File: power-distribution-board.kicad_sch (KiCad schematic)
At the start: 18 parts, among them J1 703W-00_52, J10 12V, J11 12V, J12 12V, J13 12V, J14 12V, J15 5V, J16 5V, J17 5V, J2 Screw_Terminal_01x03, J3 Screw_Terminal_01x03, J4 Screw_Terminal_01x03, J5 12V, J6 12V, J7 12V, J8 12V, J9 12V, U1 IP2721

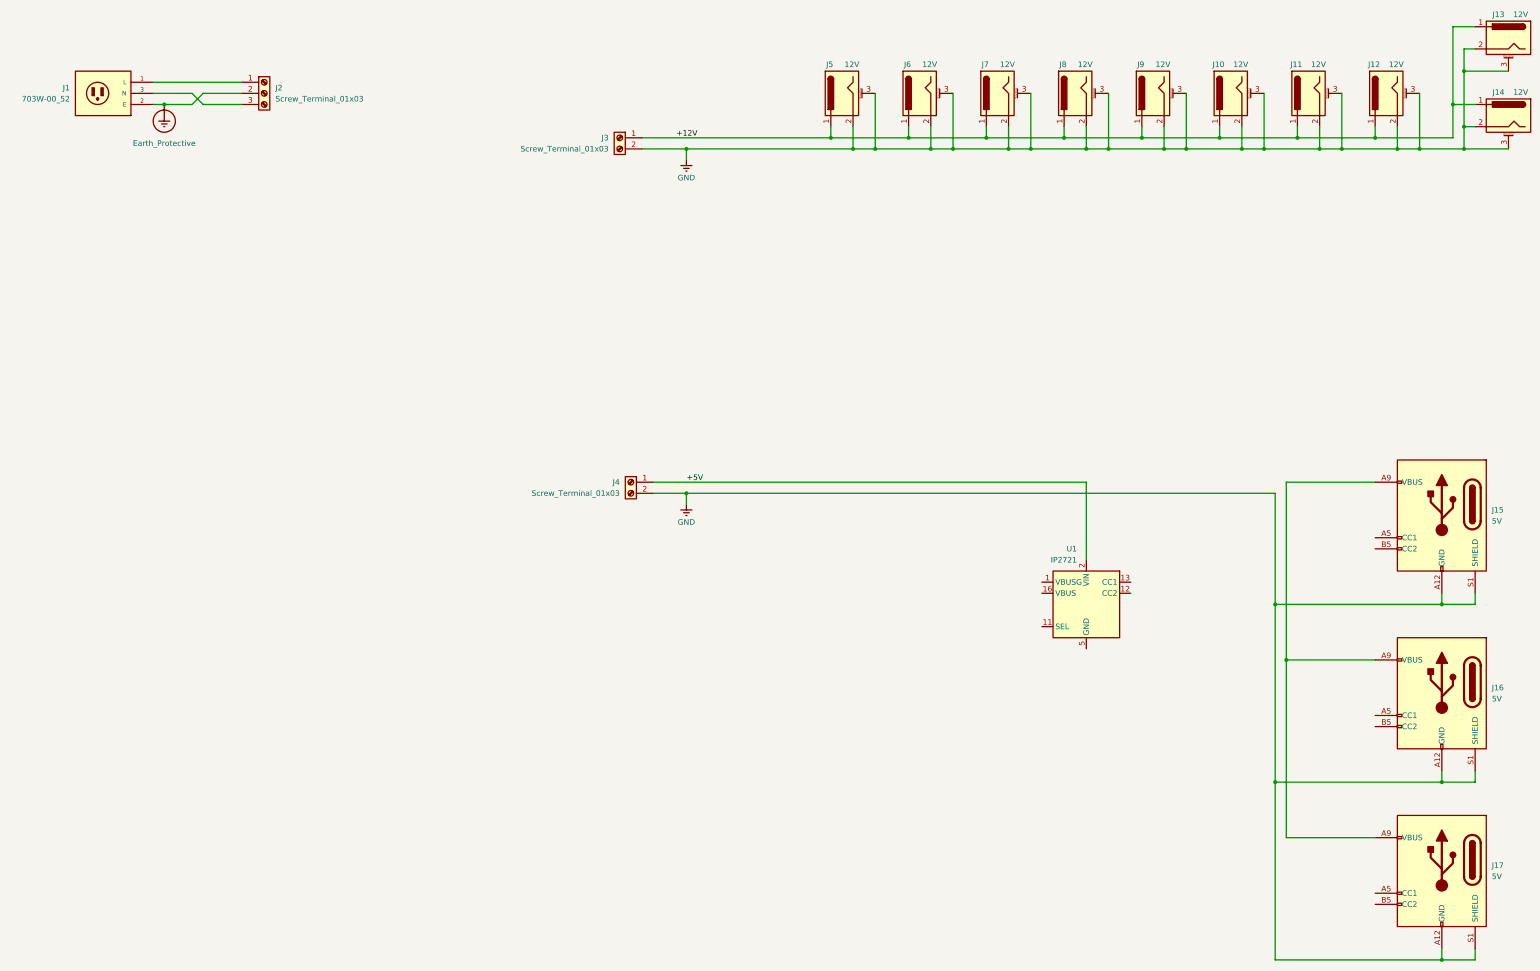
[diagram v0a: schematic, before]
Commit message: feat: align J4 block and move U2/J16 block down 1 GU
Layout alignment improvements:
- J4 screw terminal (power input) moved up 6 GU so pin 1 aligns
  with U1 IN pin row (y=116.84), treating J4+GND Earth as a block
- U2/J16 block moved down 1 GU (+2.54mm) to create ≥2 GU clearance
  between J15 Earth symbol and J16 VBUS bus (was 1 GU, now 2 GU)
- EN bus extended to span J4 tap → U2 EN (y=116.84 to y=165.10)
- All connected wires, junctions, symbols, and labels updated
- New junctions at EN bus T-points (215.9, 116.84) and (215.9, 127.00)

Co-Authored-By: Claude Sonnet 4.6 <noreply@anthropic.com>
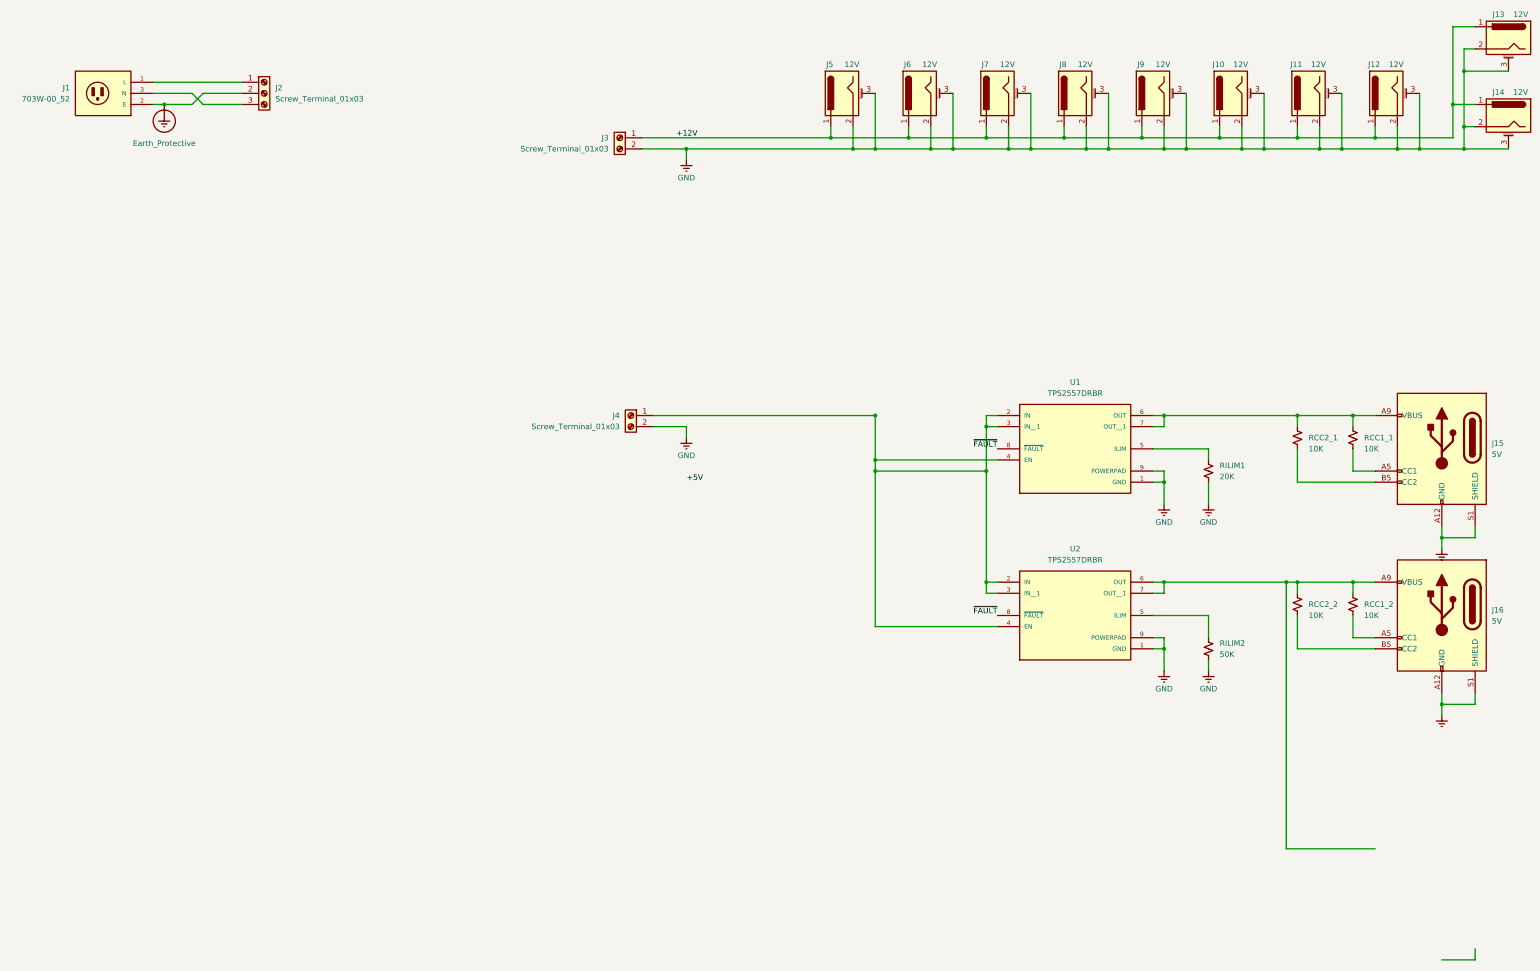
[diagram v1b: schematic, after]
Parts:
- removed J17: 5V, symbol Connector:USB_C_Receptacle_PowerOnly_6P
- removed U1: IP2721, Package_SO:TSSOP-16_4.4x5mm_P0.65mm, symbol Interface_USB:IP2721
- added RCC1_1, RCC1_2, RCC2_1, RCC2_2: 10K, Resistor_SMD:R_0603_1608Metric, symbol Device:R_Small_US
- added RILIM1: 20K, Resistor_SMD:R_0603_1608Metric, symbol Device:R_Small_US
- added RILIM2: 50K, Resistor_SMD:R_0603_1608Metric, symbol Device:R_Small_US
- added U1, U2: TPS2557DRBR, Package_DFN_QFN:DFN-8-1EP_3x3mm_P0.65mm_EP1.6x2.56mm_ThermalVias, symbol Library:TPS2557DRBR
- J15, J16: footprint (none) -> Connector_USB:USB_C_Receptacle_HRO_TYPE-C-31-M-17; LCSC (none) -> C456012; MF (none) -> SHOU HAN; MPN (none) -> TYPE-C 6P
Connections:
- net +5V: no longer J4.1 (Pin_1)
- net GND: now also RILIM1.2, RILIM2.2, U1.1 (GND), U1.9 (POWERPAD), U2.1 (GND), U2.9 (POWERPAD)
- net at J16.A5 (CC1): now also RCC1_2.2
- net at J15.A9 (VBUS), J15.B9 (VBUS): now also RCC1_1.1, RCC2_1.1, U1.6 (OUT), U1.7 (OUT__1); no longer J16.A9 (VBUS), J16.B9 (VBUS)
- net at J16.B5 (CC2): now also RCC2_2.2
- net at J15.A5 (CC1): now also RCC1_1.2
- net at J15.B5 (CC2): now also RCC2_1.2
- new net: J16.A9 (VBUS), J16.B9 (VBUS), RCC1_2.1, RCC2_2.1, U2.6 (OUT), U2.7 (OUT__1)
- new net: RILIM2.1, U2.5 (ILIM)
- new net: J4.1 (Pin_1), U1.2 (IN), U1.3 (IN__1), U1.4 (EN), U2.2 (IN), U2.3 (IN__1), U2.4 (EN)
- new net: RILIM1.1, U1.5 (ILIM)
- new net ~{FAULT}: U1.8 (~{FAULT}), U2.8 (~{FAULT})
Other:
- moved on the sheet: J15, J16, J4

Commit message: fix: correct net labels per schematic guidelines
- Rename duplicate ~{FAULT} labels to unique ~{FAULT_U1} and ~{FAULT_U2}
  (U1 pin 8 and U2 pin 8 must be on separate nets)
- Move both FAULT labels off pin connection points onto 2 GU wire stubs
  (238.76 ← 243.84 at y=124.46 for U1, y=162.56 for U2)
- Fix stranded +5V label: restore to J4 wire after J4 block move
  (y 132.08 → 116.84, matching J4 pin 1 wire at new position)

Co-Authored-By: Claude Sonnet 4.6 <noreply@anthropic.com>
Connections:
- net +5V: now also J4.1 (Pin_1), U1.2 (IN), U1.3 (IN__1), U1.4 (EN), U2.2 (IN), U2.3 (IN__1), U2.4 (EN)
- net ~{FAULT} renamed ~{FAULT_U1}
- net ~{FAULT_U1}: no longer U2.8 (~{FAULT})
- new net ~{FAULT_U2}: U2.8 (~{FAULT})
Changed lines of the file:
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@@
 	)
 	(label "+5V"
-		(at 176.53 132.08 180)
+		(at 176.53 116.84 180)
 		(effects
 			(font
@@
 		)
 	)
-	(label "~{FAULT}"
-		(at 243.84 162.56 180)
+	(label "~{FAULT_U2}"
+		(at 238.76 162.56 180)
 		(effects
 			(font
@@
 		(uuid "r1gnd000-0000-0000-0000-000000000001")
 	)
-	(label "~{FAULT}"
-		(at 243.84 124.46 180)
+	(label "~{FAULT_U1}"
+		(at 238.76 124.46 180)
 		(effects
 			(font
@@
 		(uuid "j4move00-0000-0000-0000-000000000002")
 	)
+	(wire
+		(pts (xy 243.84 124.46) (xy 238.76 124.46))
+		(stroke (width 0) (type default))
+		(uuid "faultu10-0000-0000-0000-000000000001")
+	)
+	(wire
+		(pts (xy 243.84 162.56) (xy 238.76 162.56))
+		(stroke (width 0) (type default))
+		(uuid "faultu20-0000-0000-0000-000000000001")
+	)
 )

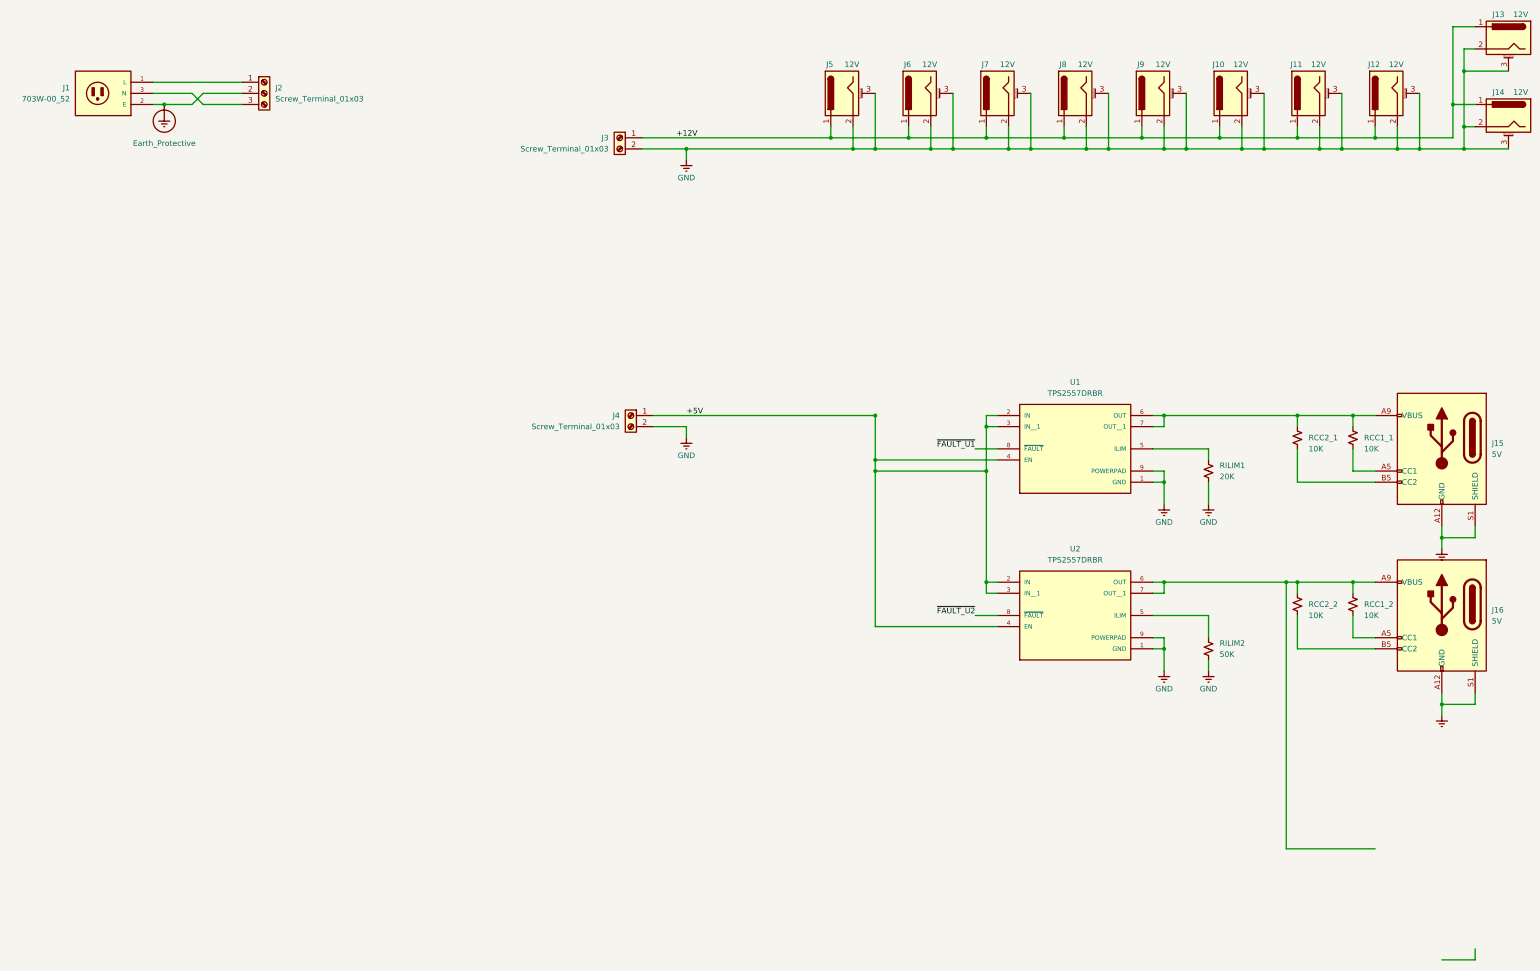
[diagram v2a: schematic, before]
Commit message: feat: add AC_L and AC_N net labels to mains conductors
Places explicit net labels on the J1→J2 AC Line and Neutral wires,
activating the Mains_AC net class (3.0mm clearance) for those nets.

Remaining: +5V_J15 / +5V_J16 labels on U1/U2 output wires pending.

Co-Authored-By: Claude Sonnet 4.6 <noreply@anthropic.com>
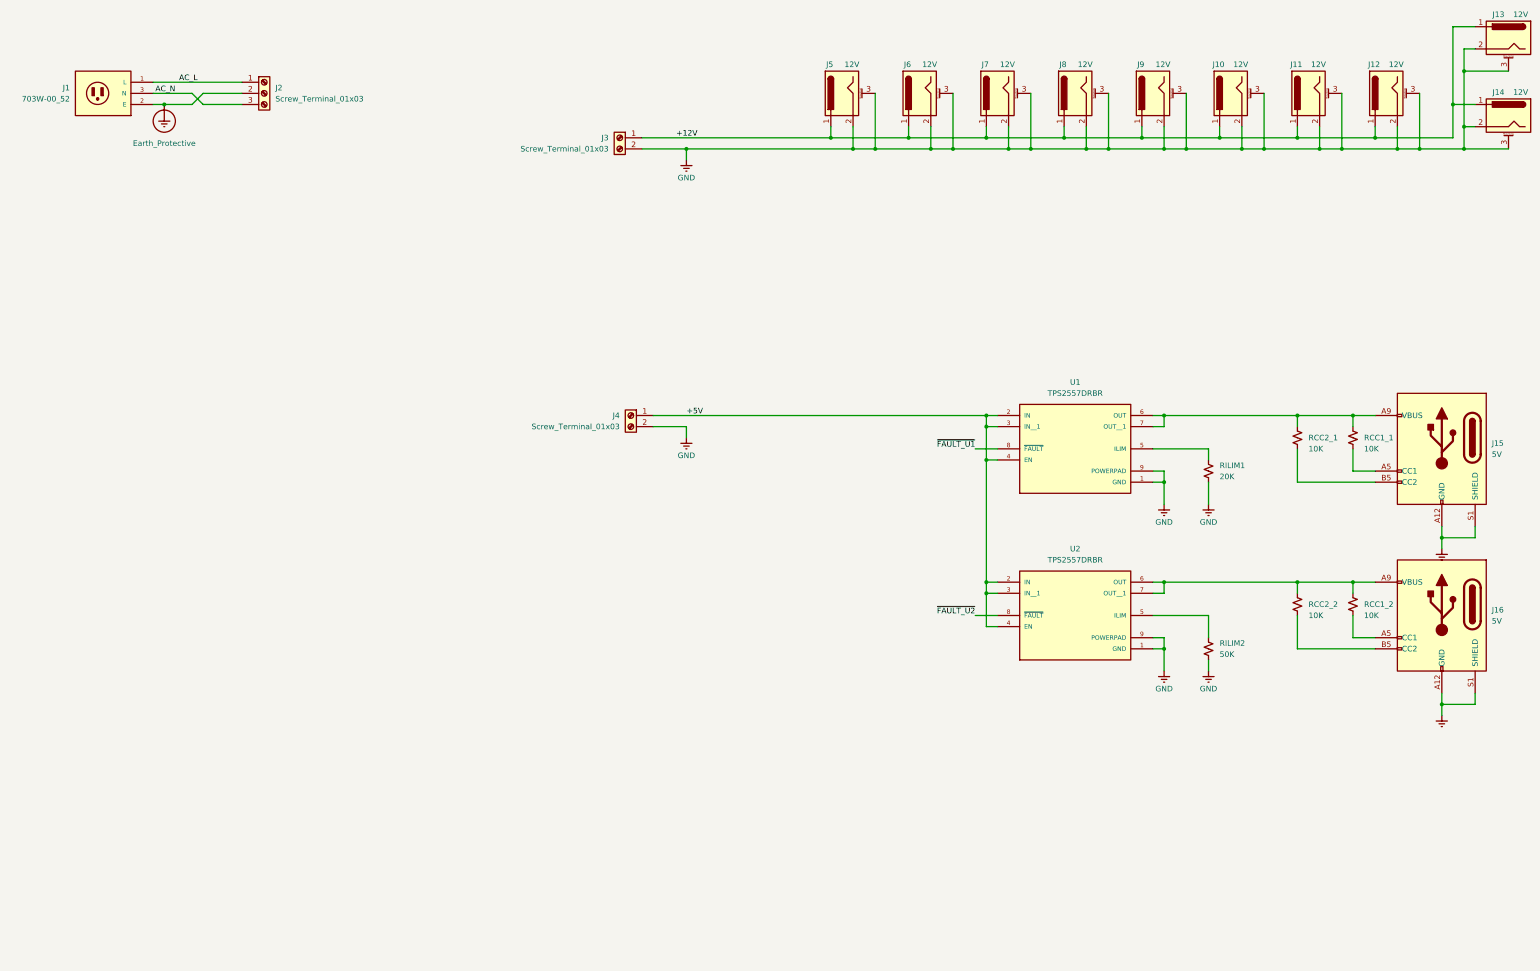
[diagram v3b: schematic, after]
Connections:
- net AC_L: now reaches J1.1 (L), J2.1 (Pin_1)
- net AC_N: now reaches J1.3 (N), J2.3 (Pin_3)
